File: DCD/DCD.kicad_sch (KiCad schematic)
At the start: 0 parts

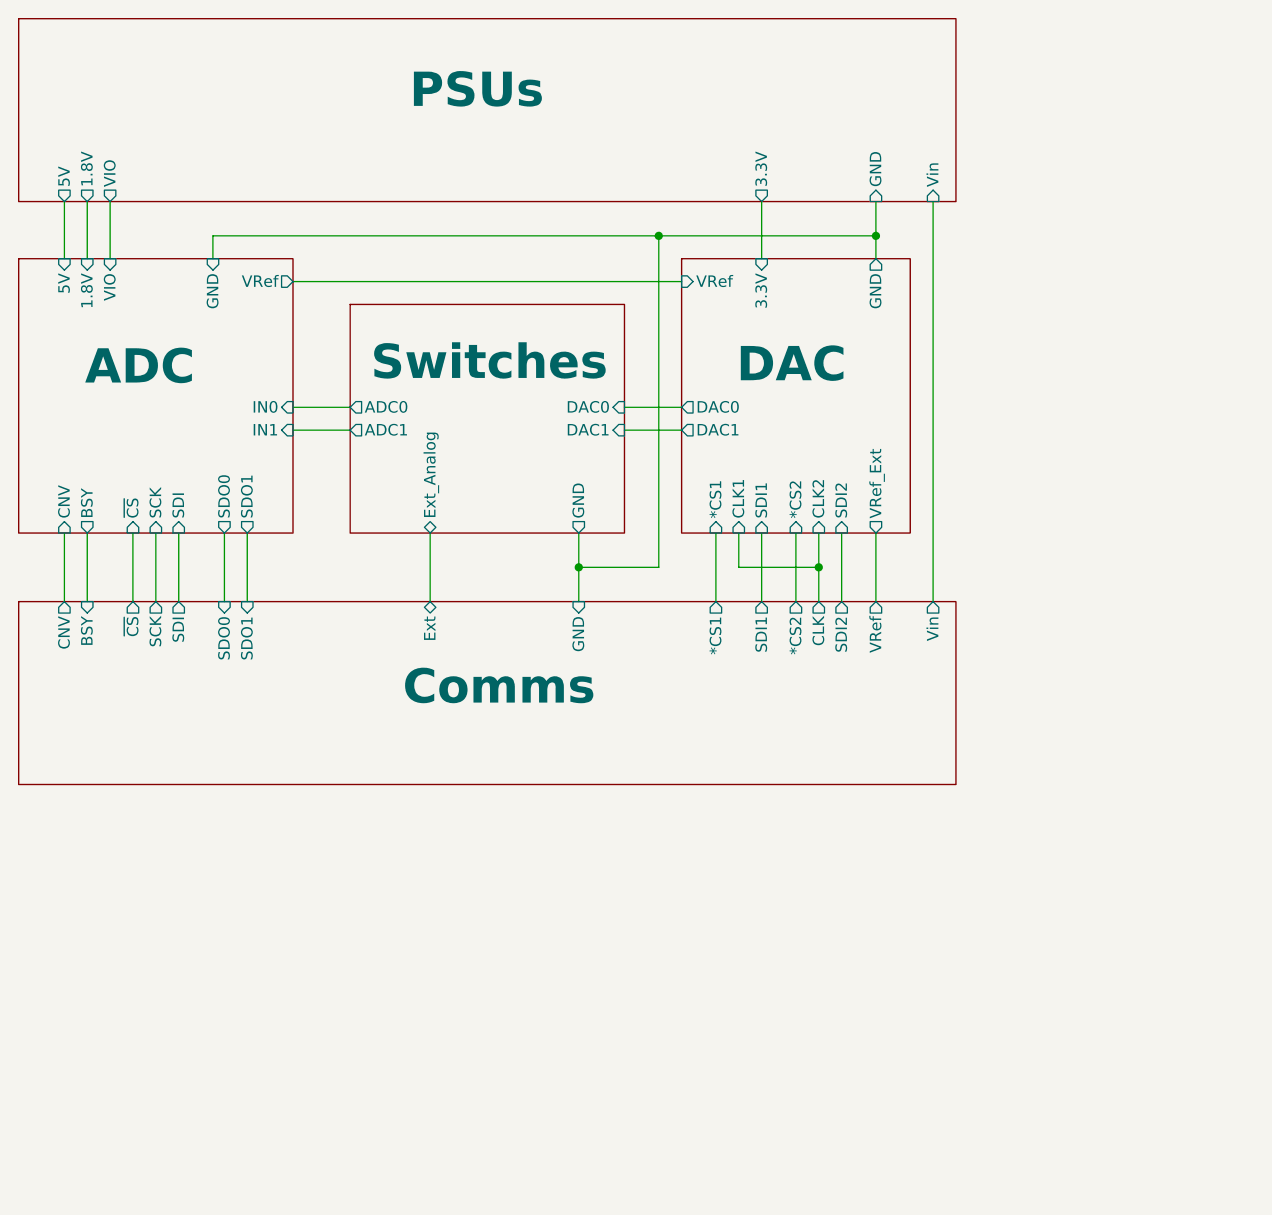
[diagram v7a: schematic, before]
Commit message: Finished
Final touches, PSUs filtering, external connections, psu connections for
the negative voltage, and the DAC higher voltage, and the negative
voltage. Added an external connection directely to the DAC.
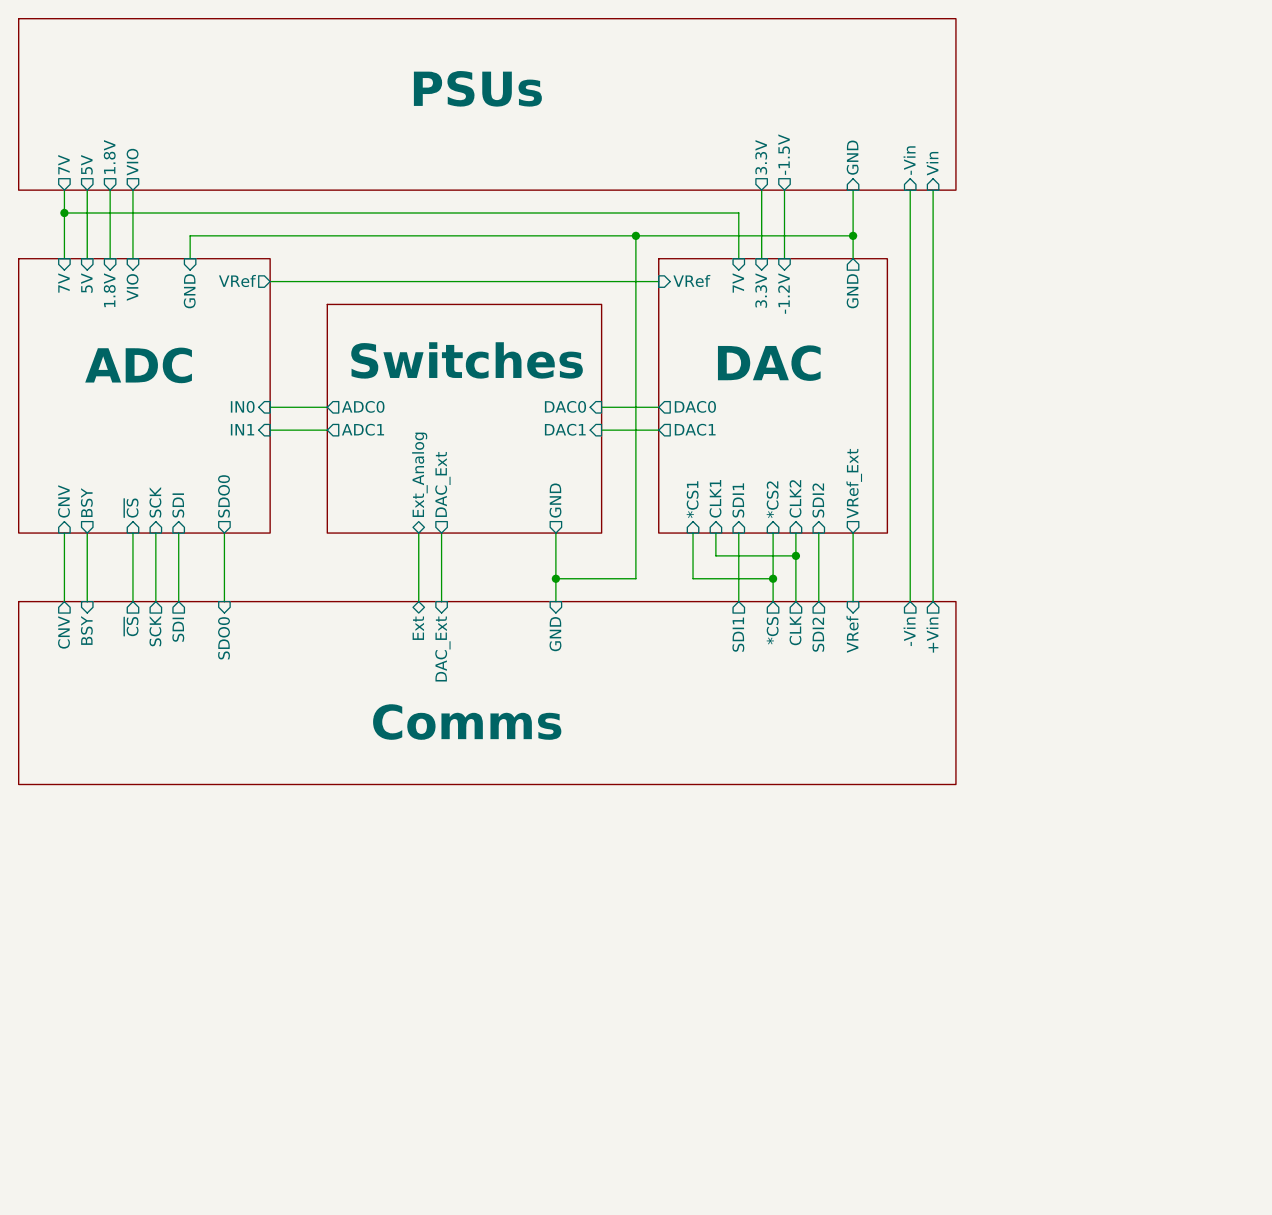
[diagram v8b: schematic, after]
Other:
- sheet ADC ports: added 7V; removed SDO1
- sheet Comms ports: added *CS, +Vin, -Vin, DAC_Ext; removed *CS1, *CS2, SDO1, Vin
- sheet DAC ports: added -1.2V, 7V; removed none
- sheet PSUs ports: added -1.5V, -Vin, 7V; removed none
- sheet Switches ports: added DAC_Ext; removed none
